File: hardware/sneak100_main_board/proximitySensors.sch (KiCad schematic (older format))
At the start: 29 parts, among them Q1 Q_Photo_NPN_CE, U1 CD4051B, U2 CD4051B

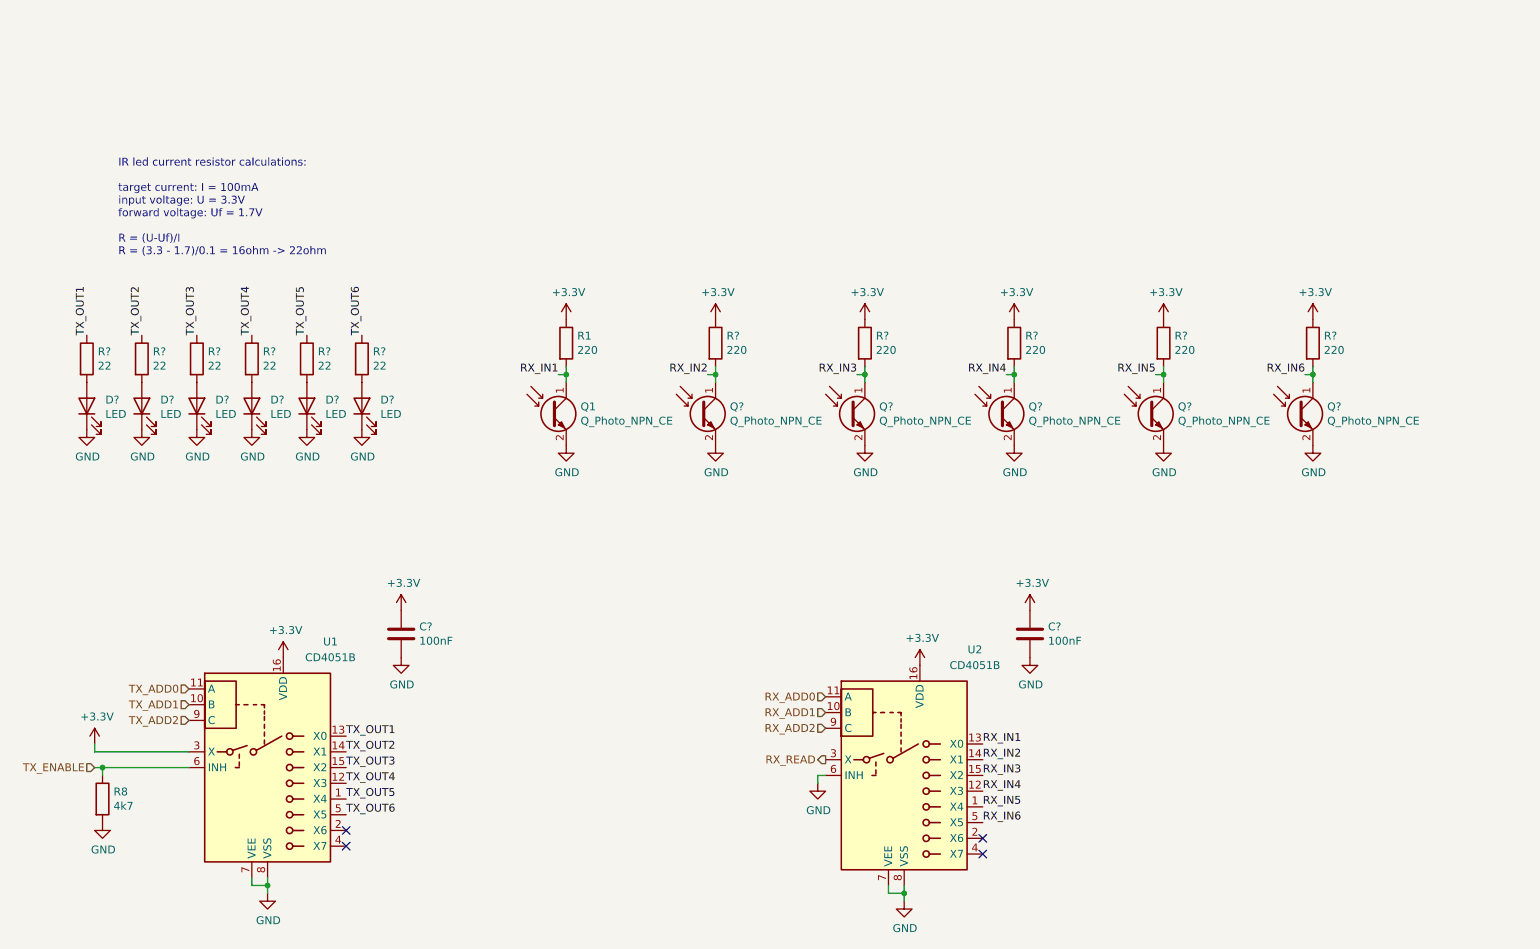
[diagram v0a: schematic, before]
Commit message: User buttons, leds and uart
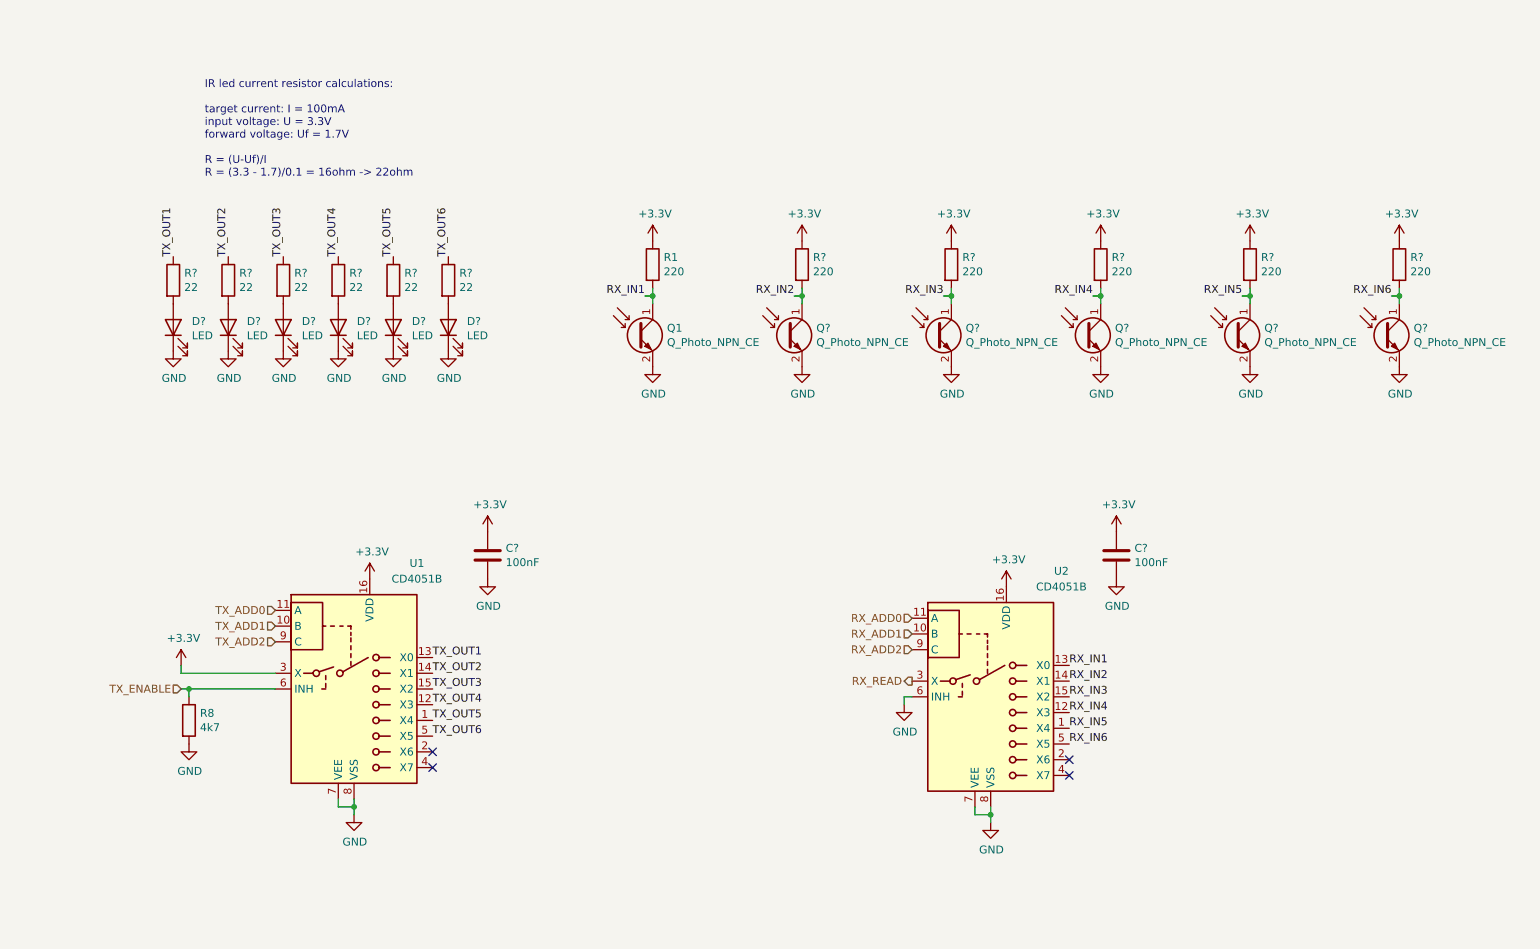
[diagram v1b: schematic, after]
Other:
- moved on the sheet: C?, D?, Q1, Q?, R1, R8, R?, U1, U2

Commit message: Proximity sensor first test
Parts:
- D4, D5, D6, D7, D8, D9: renamed from D?; value LED -> SFH4550
- Q1: value Q_Photo_NPN_CE -> SFH-313FA
- Q2, Q3, Q4, Q5, Q6: renamed from Q?; value Q_Photo_NPN_CE -> SFH-313FA
- R10, R11, R7, R8, R9: renamed from R?; value 220 -> 10k
- R12, R13, R14, R15, R16, R17: renamed from R?; value 22 -> 20
- R6: renamed from R1; value 220 -> 10k
- gave numbers to parts that had none: 2
- renumbered R8 to R18
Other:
- moved on the sheet: D4, D5, D6, D7, D8, D9, Q1, Q2, Q3, Q4, Q5, Q6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

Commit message: motors circuit scheme
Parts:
- C11: renamed from C3; footprint (none) -> Capacitor_SMD:C_0805_2012Metric
- C12: renamed from C4; footprint (none) -> Capacitor_SMD:C_0805_2012Metric
- D4, D5, D6, D7, D8, D9, Q1, Q2, Q3, Q4, Q5, Q6: footprint (none) -> Connector_PinHeader_2.54mm:PinHeader_1x02_P2.54mm_Vertical
- R10, R11, R12, R13, R14, R15, R16, R17, R18, R6, R7, R8, R9: footprint (none) -> Resistor_SMD:R_0805_2012Metric
- U5: renamed from U1; footprint (none) -> Package_SO:SOIC-16_3.9x9.9mm_P1.27mm
- U6: renamed from U2; footprint (none) -> Package_SO:SOIC-16_3.9x9.9mm_P1.27mm
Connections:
- net TX_ADD0 is gone; now on net ADD0: U5.11 (A)
- net TX_ADD1 is gone; now on net ADD1: U5.10 (B)
- net TX_ADD2 is gone; now on net ADD2: U5.9 (C)
- net RX_ADD0 renamed ADD0
- net RX_ADD1 renamed ADD1
- net RX_ADD2 renamed ADD2
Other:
- note added: "Receivers"
- note added: "Transmitters"
- moved on the sheet: C11, C12, Q1, Q2, Q3, Q4, Q5, Q6, R10, R11, R18, R6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

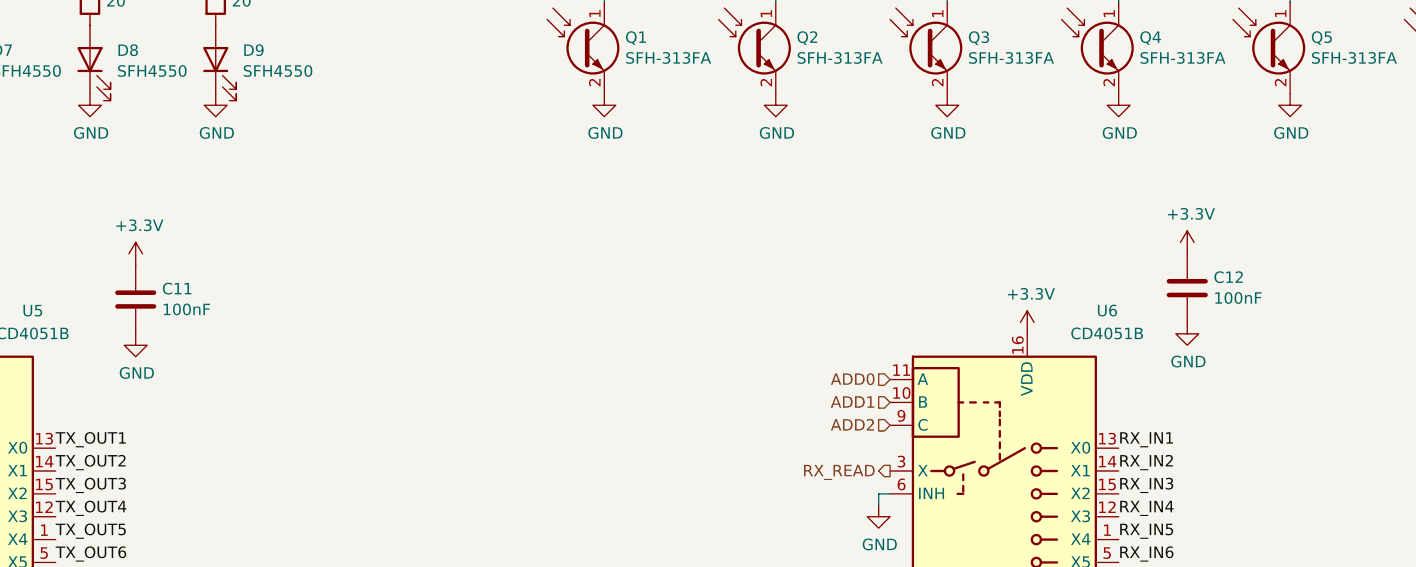
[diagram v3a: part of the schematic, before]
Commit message: Add stm32f405 uC scheme
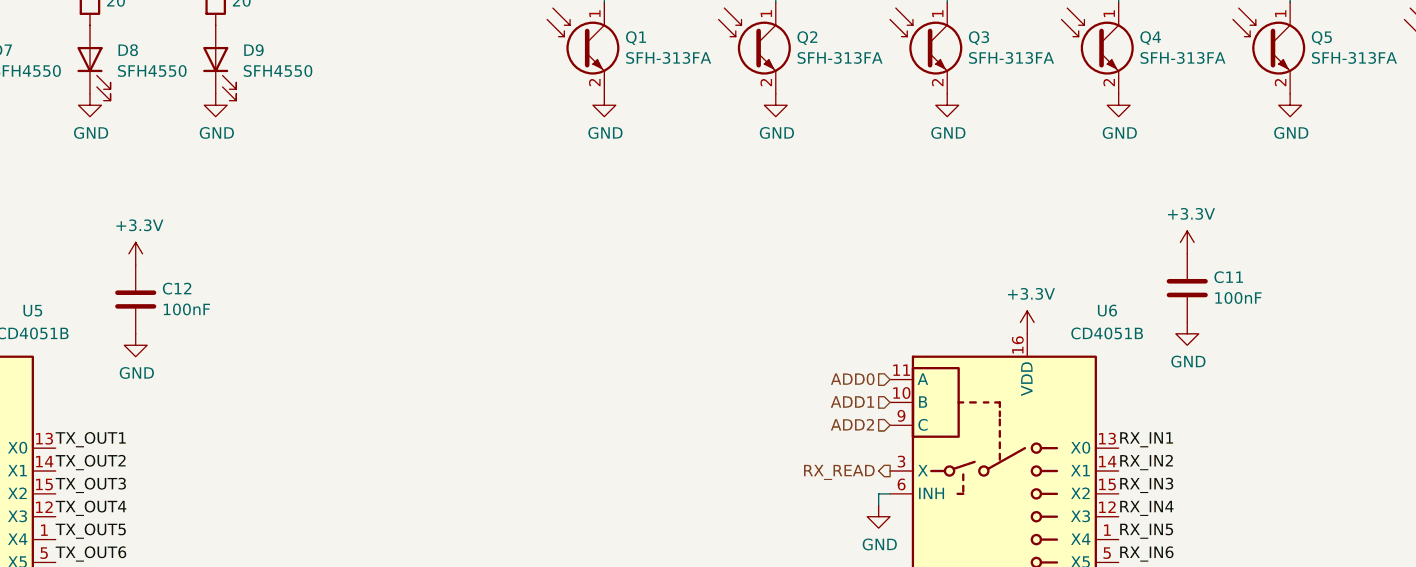
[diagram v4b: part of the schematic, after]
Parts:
- renumbered C12 to C11, C11 to C12
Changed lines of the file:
@@
 $Descr A4 11693 8268
 encoding utf-8
-Sheet 6 7
+Sheet 5 7
 Title ""
 Date ""
@@
 $EndComp
 $Comp
-L power:+3.3V #PWR063
+L power:+3.3V #PWR064
 U 1 1 60E248E2
 P 3200 4100
-F 0 "#PWR063" H 3200 3950 50  0001 C CNN
+F 0 "#PWR064" H 3200 3950 50  0001 C CNN
 F 1 "+3.3V" H 3215 4273 50  0000 C CNN
 F 2 "" H 3200 4100 50  0001 C CNN
@@
 TX_OUT6
 $Comp
-L Device:C C11
+L Device:C C12
 U 1 1 60F1A0B6
 P 3950 3950
-F 0 "C11" H 4065 3996 50  0000 L CNN
+F 0 "C12" H 4065 3996 50  0000 L CNN
 F 1 "100nF" H 4065 3905 50  0000 L CNN
 F 2 "Capacitor_SMD:C_0805_2012Metric" H 3988 3800 50  0001 C CNN
@@
 $EndComp
 $Comp
-L power:+3.3V #PWR061
+L power:+3.3V #PWR062
 U 1 1 60F1B962
 P 3950 3800
-F 0 "#PWR061" H 3950 3650 50  0001 C CNN
+F 0 "#PWR062" H 3950 3650 50  0001 C CNN
 F 1 "+3.3V" H 3965 3973 50  0000 C CNN
 F 2 "" H 3950 3800 50  0001 C CNN
@@
 $EndComp
 $Comp
-L power:GND #PWR064
+L power:GND #PWR065
 U 1 1 60F1BF31
 P 3950 4100
-F 0 "#PWR064" H 3950 3850 50  0001 C CNN
+F 0 "#PWR065" H 3950 3850 50  0001 C CNN
 F 1 "GND" H 3955 3927 50  0000 C CNN
 F 2 "" H 3950 4100 50  0001 C CNN
@@
 $EndComp
 $Comp
-L Device:C C12
+L Device:C C11
 U 1 1 60F1EDF8
 P 8550 3900
-F 0 "C12" H 8665 3946 50  0000 L CNN
+F 0 "C11" H 8665 3946 50  0000 L CNN
 F 1 "100nF" H 8665 3855 50  0000 L CNN
 F 2 "Capacitor_SMD:C_0805_2012Metric" H 8588 3750 50  0001 C CNN
@@
 $EndComp
 $Comp
-L power:+3.3V #PWR062
+L power:+3.3V #PWR061
 U 1 1 60F1EDFE
 P 8550 3750
-F 0 "#PWR062" H 8550 3600 50  0001 C CNN
+F 0 "#PWR061" H 8550 3600 50  0001 C CNN
 F 1 "+3.3V" H 8565 3923 50  0000 C CNN
 F 2 "" H 8550 3750 50  0001 C CNN
@@
 $EndComp
 $Comp
-L power:GND #PWR065
+L power:GND #PWR063
 U 1 1 60F1EE04
 P 8550 4050
-F 0 "#PWR065" H 8550 3800 50  0001 C CNN
+F 0 "#PWR063" H 8550 3800 50  0001 C CNN
 F 1 "GND" H 8555 3877 50  0000 C CNN
 F 2 "" H 8550 4050 50  0001 C CNN

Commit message: Hardware configuration schematic
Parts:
- renumbered C11 to C12, C12 to C13, R6 to R10, R7 to R11, R8 to R12, R9 to R13, R10 to R14, R11 to R15, R12 to R16, R13 to R17, R14 to R18, R15 to R19, R16 to R20, R17 to R21, R18 to R22, U5 to U6, U6 to U7

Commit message: Power section scheme
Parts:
- added D13: SFH203, symbol Device:D_Photo
- added R30: 200k, symbol Device:R
- C16: renamed from C12; footprint Capacitor_SMD:C_0805_2012Metric -> Capacitor_SMD:C_0603_1608Metric
- C17: renamed from C13; footprint Capacitor_SMD:C_0805_2012Metric -> Capacitor_SMD:C_0603_1608Metric
- renumbered D7 to D10, D8 to D11, D9 to D12, D4 to D7, D5 to D8, D6 to D9, Q1 to Q3, Q2 to Q4, Q3 to Q5, Q4 to Q6, Q5 to Q7, Q6 to Q8, R10 to R18, R11 to R19, R12 to R20, R13 to R21, R14 to R22, R15 to R23, R16 to R24, R17 to R25, R18 to R26, R19 to R27, R20 to R28, R21 to R29, R22 to R31, U6 to U7, U7 to U8
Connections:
- wire segments 33 -> 36
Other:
- note added: "IR led current resistor calculations:\n\ntarget current: I = 100mA\ninput voltage: U = 3.3V\nforward voltage: Uf = 1.7V\n\nR = (U-Uf)/I\nR = (3.3 - 1.7)/0.1 = 16ohm -> 20ohm"
- note removed: "IR led current resistor calculations:\n\ntarget current: I = 100mA\ninput voltage: U = 3.3V\nforward voltage: Uf = 1.7V\n\nR = (U-Uf)/I\nR = (3.3 - 1.7)/0.1 = 16ohm -> 22ohm"

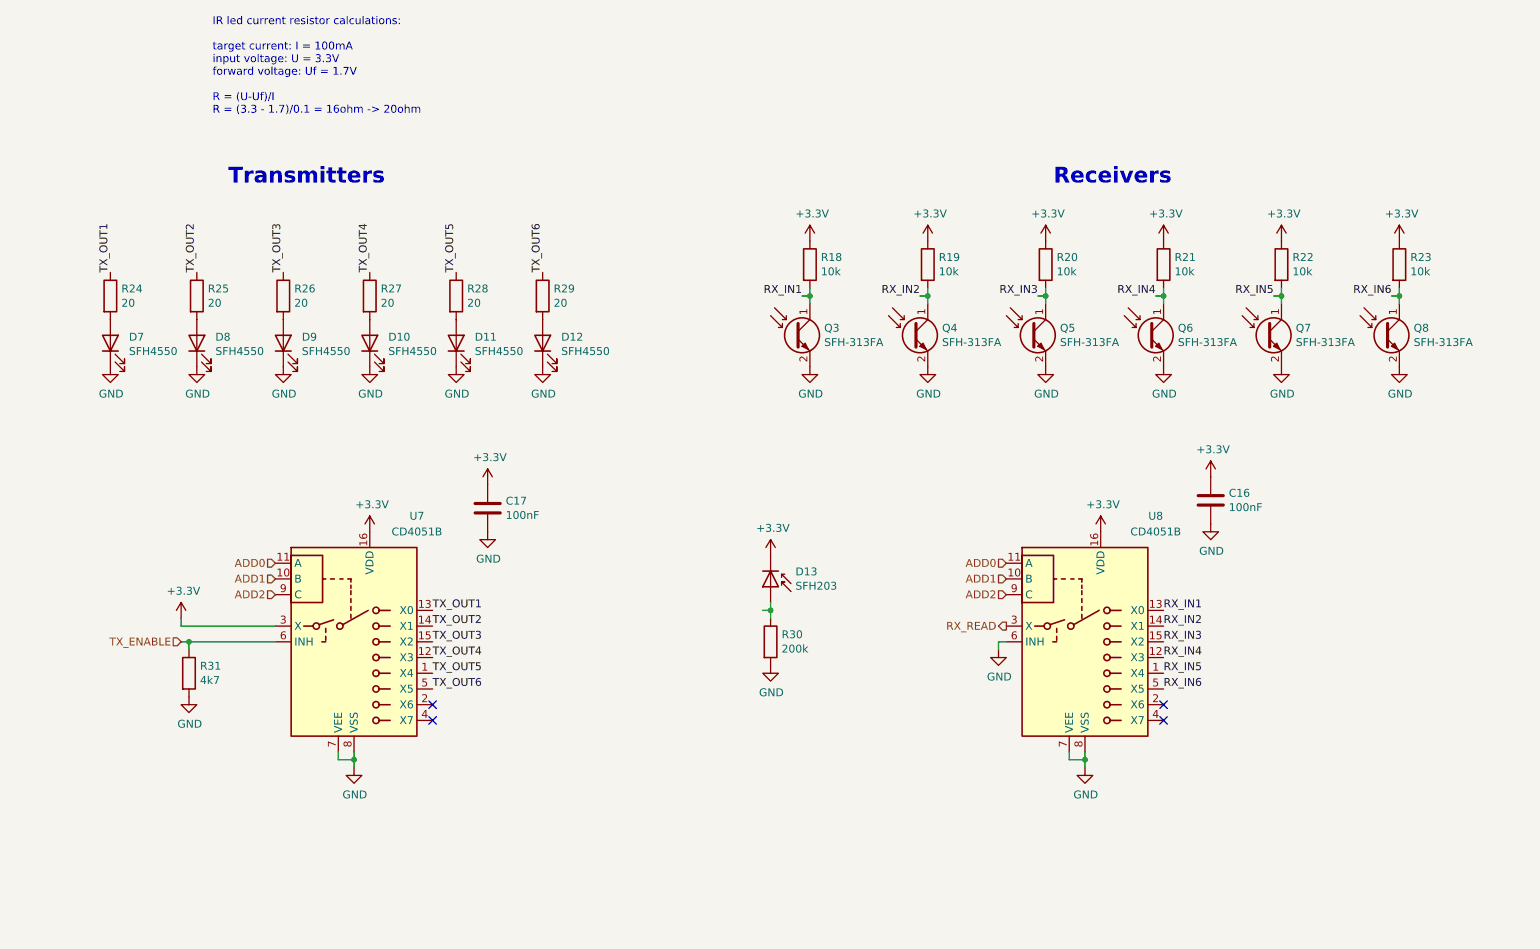
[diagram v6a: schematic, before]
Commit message: USB FDU mode
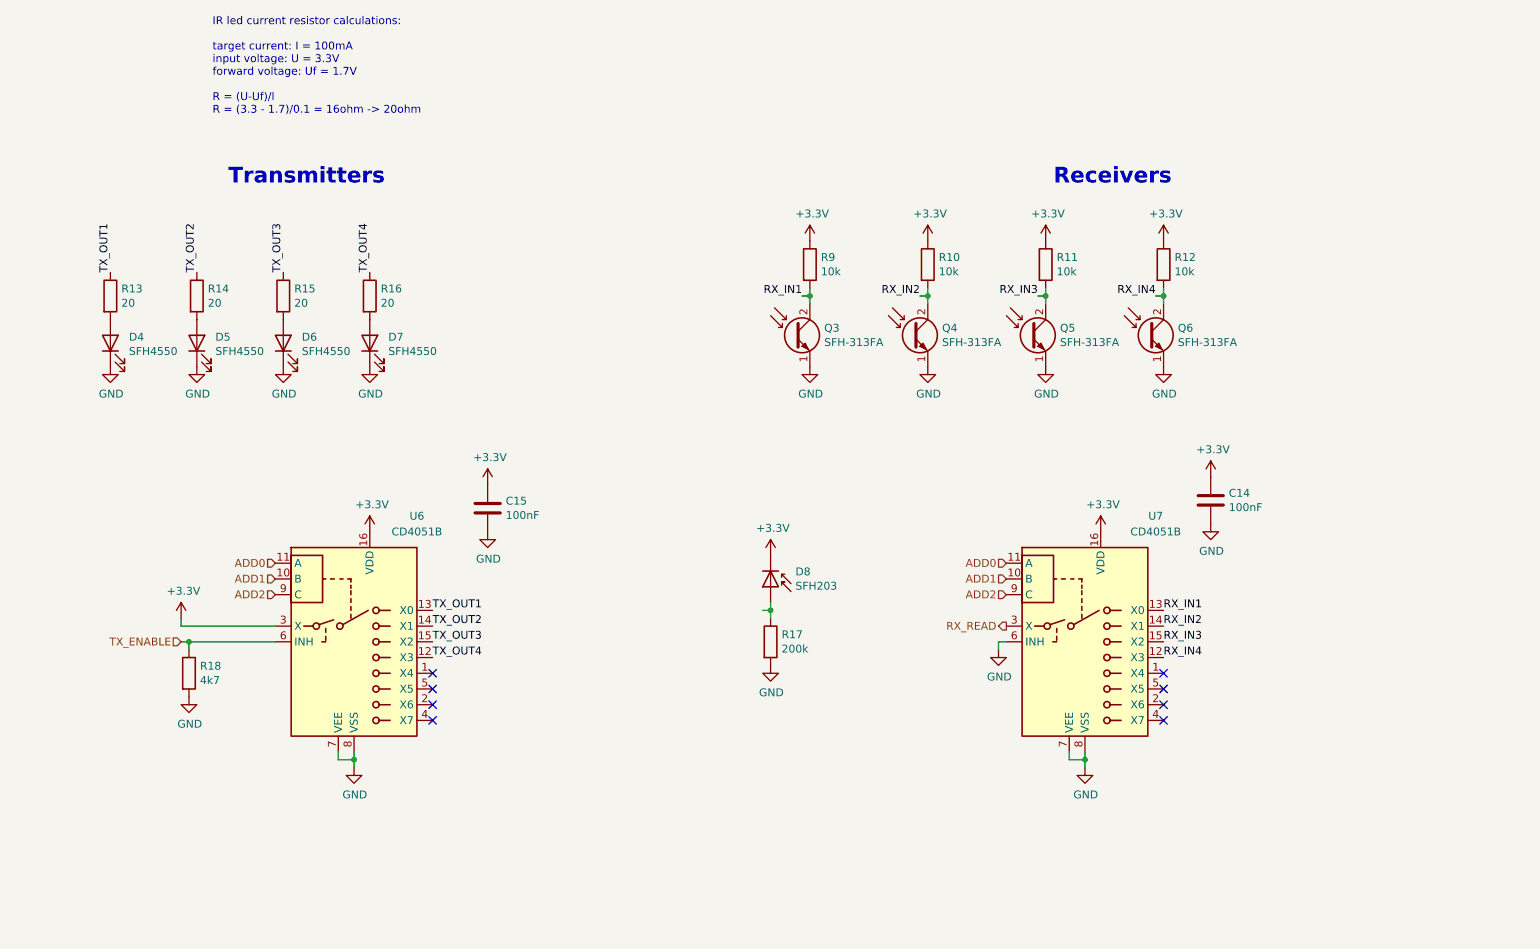
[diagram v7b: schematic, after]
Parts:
- removed D11, D12: SFH4550, Connector_PinHeader_2.54mm:PinHeader_1x02_P2.54mm_Vertical, symbol Device:LED
- removed Q3, Q4, Q5, Q6, Q7, Q8: SFH-313FA, Connector_PinHeader_2.54mm:PinHeader_1x02_P2.54mm_Vertical, symbol Device:Q_Photo_NPN_CE
- removed R22, R23: 10k, Resistor_SMD:R_0805_2012Metric, symbol Device:R
- removed R28, R29: 20, Resistor_SMD:R_0805_2012Metric, symbol Device:R
- added Q3, Q4, Q5, Q6: SFH-313FA, Connector_PinHeader_2.54mm:PinHeader_1x02_P2.54mm_Vertical, symbol Device:Q_Photo_NPN_EC
- renumbered C16 to C14, C17 to C15, D7 to D4, D8 to D5, D9 to D6, D10 to D7, D13 to D8, R19 to R10, R20 to R11, R21 to R12, R24 to R13, R25 to R14, R26 to R15, R27 to R16, R30 to R17, R31 to R18, R18 to R9, U7 to U6, U8 to U7
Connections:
- net labels removed: RX_IN5, RX_IN6, TX_OUT5, TX_OUT6
- wire segments 36 -> 30
- no-connect marks 4 -> 8
